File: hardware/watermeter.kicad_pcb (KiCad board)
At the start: 2 copper layers, 105 x 90 mm, 69 parts, among them J1 Screw_Terminal_01x03, J10 SRD-05VDC-SL-C, J11 SRD-05VDC-SL-C, J2 Screw_Terminal_01x03, J3 Conn_01x08_Pin, J4 Conn_01x08_Pin, J5 TC2030, J6 Screw_Terminal_01x02, J7 USB-TYPE-C-31-M-12, J8 Screw_Terminal_01x02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

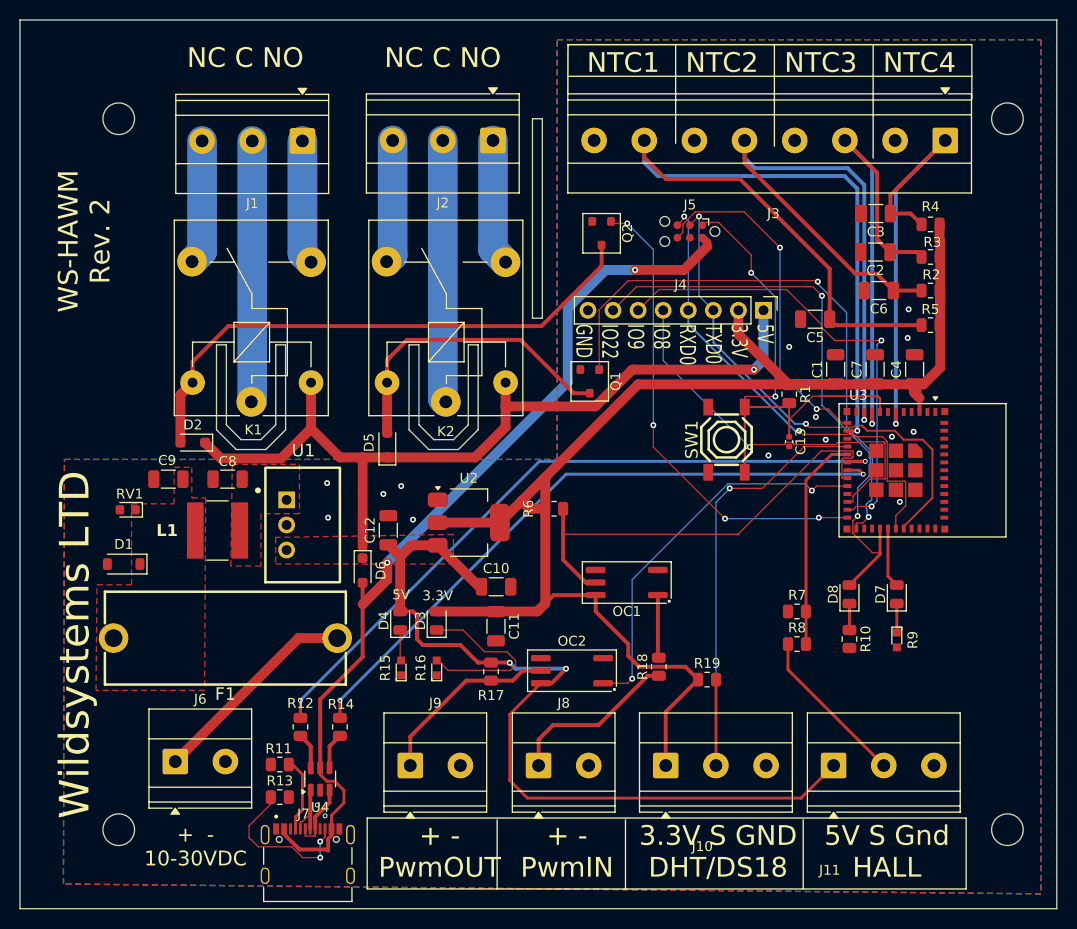
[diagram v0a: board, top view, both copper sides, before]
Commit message: Production - V2 Added: TagConnect port for fast firmware upload Fixes: Resistive diider fo hall sensor was replaced with transistor logic Refactoring for whole power supply Minimal track width 0.2mm Fixed digital transistor pin swap
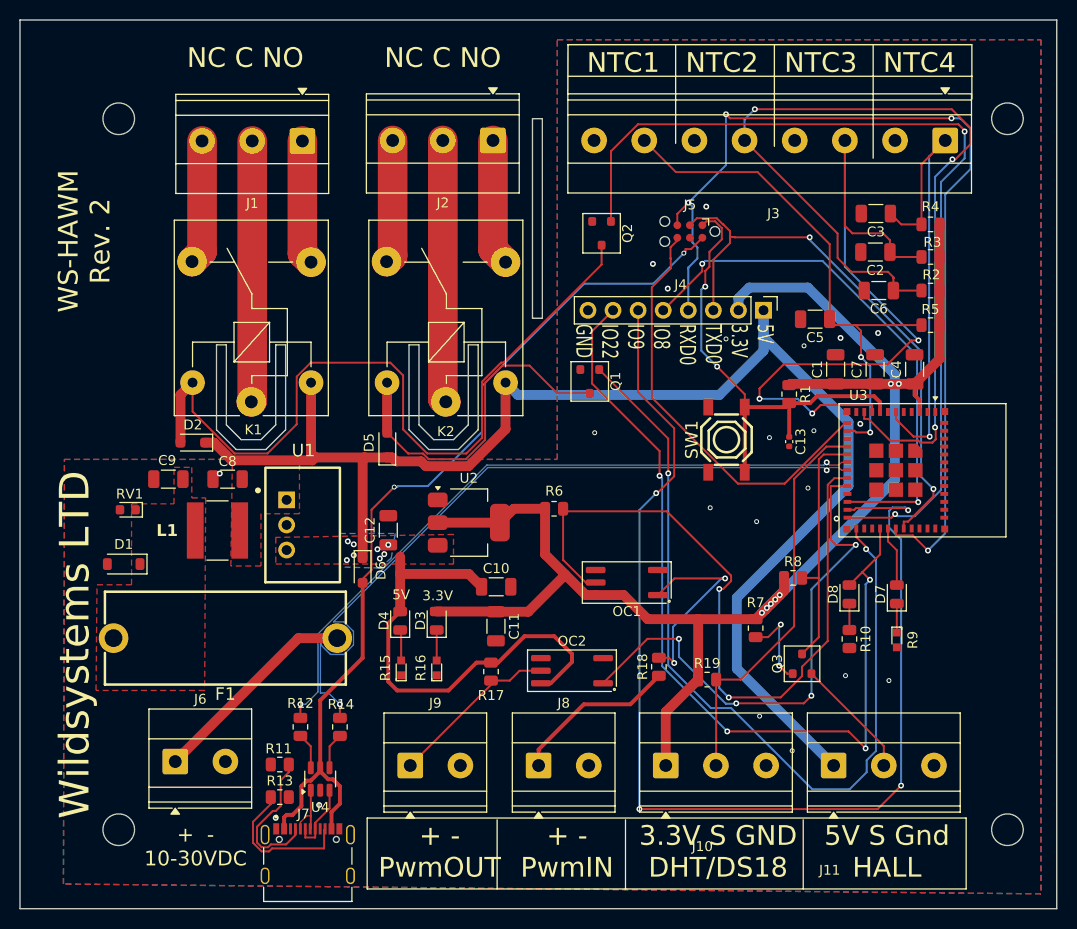
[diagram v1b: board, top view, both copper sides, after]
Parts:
- added Q3: MMBT2222A, PCM_Package_TO_SOT_SMD_AKL:SOT-23, F.Cu at (164.7, 116.2)
- R7: value 2k -> 10K
- R8: value 1k -> 10K
- moved R8 6.71 mm to (163.8, 107.5)
- moved R7 4.51 mm to (160.0, 112.6), turned to -90 degrees
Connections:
- J11 pad 2: Net-(J10-Pin_2) -> Net-(J11-Pin_2)
- R7 pad 1: /IO7 -> +3.3V
- R7 pad 2: GND -> Net-(Q3-B)
- R8 pad 1: Net-(J10-Pin_2) -> +3.3V
- R8 pad 2: /IO7 -> /~{IO7}
- U3 pad 16: /IO7 -> /~{IO7}
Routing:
- net /IO9: track 47.6 -> 117.9 mm, vias 2 -> 4
- net /RXD0: track 48.3 -> 99.4 mm, vias 2 -> 4
- net /IO18: track 48.1 -> 92.5 mm, vias 4 -> 2
- net /IO1: track 90.2 -> 54.2 mm, vias 1 -> 2
- net /IO5: track 65.2 -> 95.0 mm, vias 1 -> 3
- net /IO22: track 59.9 -> 89.3 mm, vias 2 -> 4
- net /IO14: track 46.5 -> 73.7 mm, vias 0 -> 2
- net /IO19: track 58.3 -> 84.8 mm
- net /IO4: track 47.7 -> 74.0 mm, vias 1 -> 3
- net /~{IO7}: track 0.00 -> 25.2 mm
- net Net-(D2-A): track 56.2 -> 79.6 mm
- net +5V: track 173.7 -> 195.8 mm, vias 3 -> 8
- net /IO7: track 21.9 -> 0.00 mm
- net Net-(J10-Pin_2): track 16.3 -> 0.00 mm
- net Net-(D3-K): track 18.4 -> 3.09 mm
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- added copper zone on B.Cu, net +5V
